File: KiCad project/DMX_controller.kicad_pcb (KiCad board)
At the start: 2 copper layers, 139.7 x 121.9 mm, 12 parts, among them J1 DMX_output, SW1 SW_Push_DPDT, U1 TTL_to_RS485_transceiver

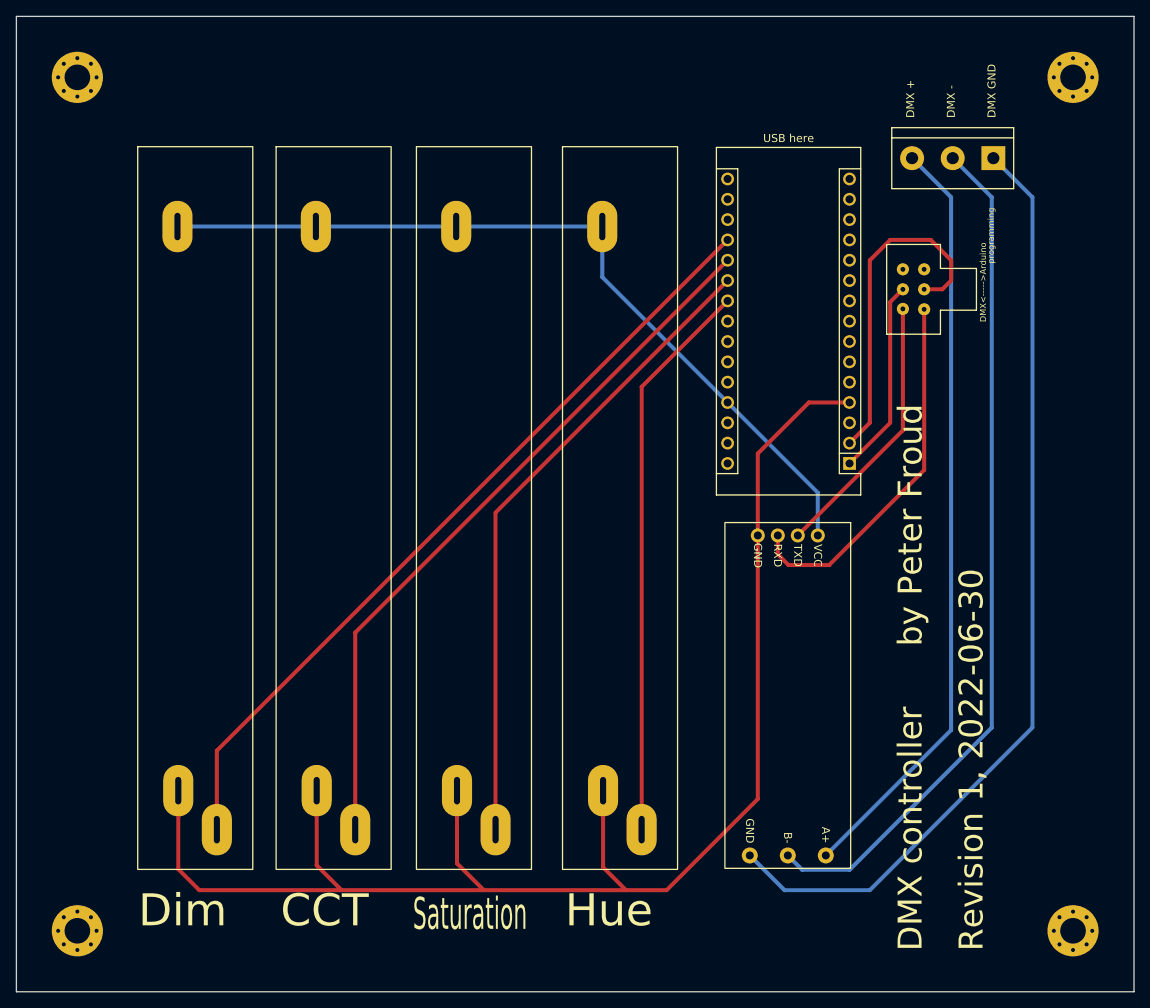
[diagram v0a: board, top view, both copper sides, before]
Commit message: Add 3D models to slide pot and screw terminal
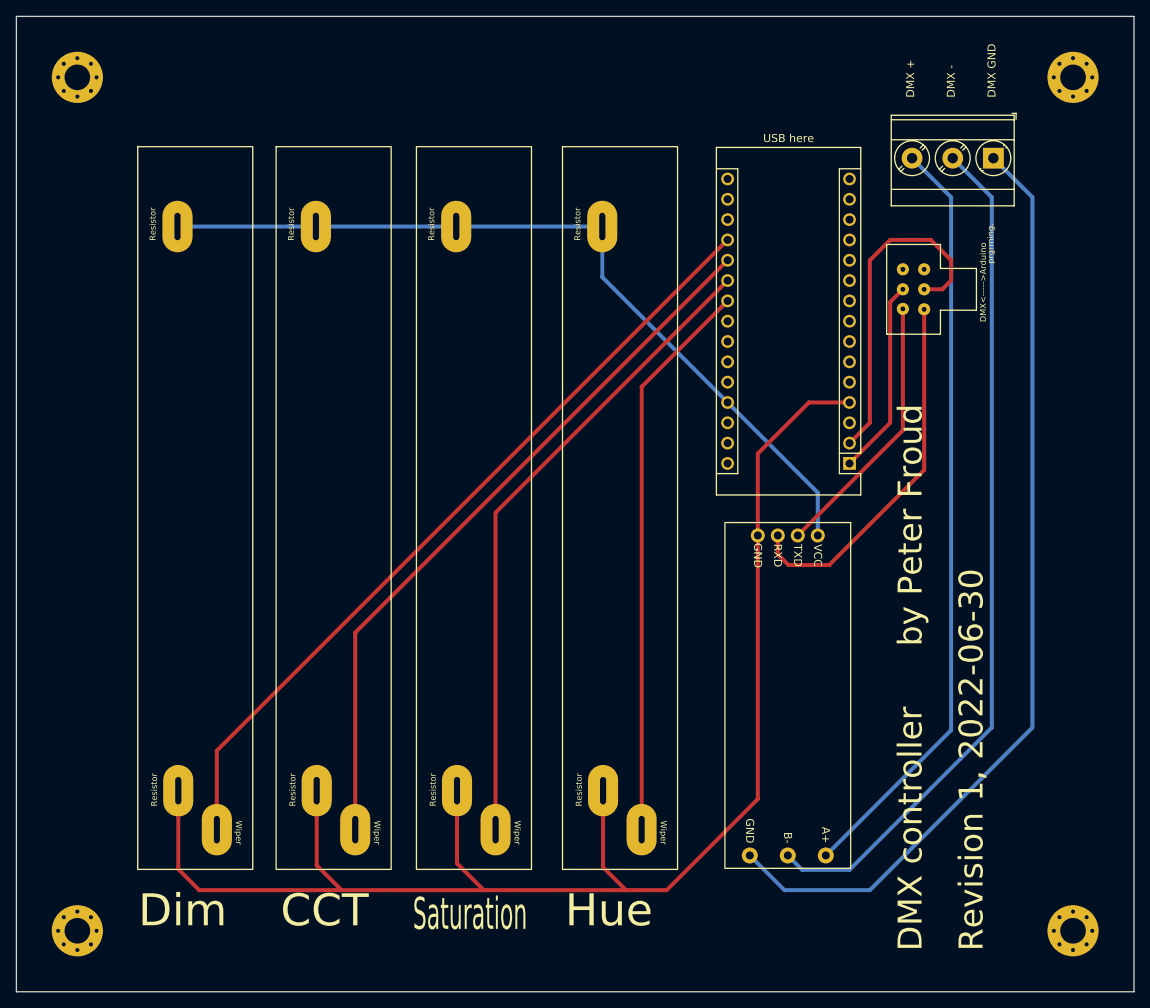
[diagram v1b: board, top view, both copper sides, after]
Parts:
- J1: footprint TerminalBlock:TerminalBlock_bornier-3_P5.08mm -> TerminalBlock_Phoenix:TerminalBlock_Phoenix_MKDS-3-3-5.08_1x03_P5.08mm_Horizontal
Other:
- board text added: "prgrming."
- board text removed: "programming"
